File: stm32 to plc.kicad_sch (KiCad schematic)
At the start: 76 parts, among them J1 Microsemi_FlashPro-JTAG-10, J13 USB_C_Receptacle_USB2.0_14P, J14 Conn_01x08_Socket, J15 Conn_01x08_Socket, J16 Conn_2Rows-09Pins, J2 Conn_01x25, Q3 DMP3013SFV, Q4 BC107, Q5 BC107, SW1 SW_Push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

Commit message: :Zap:making chngs to powerinput, and relay output
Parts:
- removed BT1: Battery_Cell, symbol Device:Battery_Cell
- removed C12: 100nF, Capacitor_Tantalum_SMD:CP_EIA-3216-18_Kemet-A, symbol Device:C
- removed C13: 2.2uF, Capacitor_Tantalum_SMD:CP_EIA-3216-18_Kemet-A, symbol Device:C
- removed D6: PMEG3010EJ, Diode_SMD:D_SOD-323F, symbol Diode:PMEG3010EJ
- removed F1: Fuse, symbol Device:Fuse
- removed Q3: DMP3013SFV, Package_SON:Diodes_PowerDI3333-8, symbol Transistor_FET:DMP3013SFV
- removed R68: 10K, Resistor_SMD:R_0201_0603Metric, symbol Device:R
- added PS1: HLK-20M24, Converter_ACDC:Converter_ACDC_Hi-Link_HLK-20Mxx, symbol Converter_ACDC:HLK-20M24
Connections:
- net OUT 5V: no longer U2.2 (OUT)
- new net OUT 3.3V: U2.2 (OUT)

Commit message: :rocket:Have added Ethernet and removed USB
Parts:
- removed FB1: FerriteBead_Small, symbol Device:FerriteBead_Small
- removed J13: USB_C_Receptacle_USB2.0_14P, Connector_USB:USB_C_Receptacle_GCT_USB4105-xx-A_16P_TopMnt_Horizontal, symbol Connector:USB_C_Receptacle_USB2.0_14P
- removed R36, R37: 10k, Resistor_SMD:R_0805_2012Metric, symbol Device:R
- removed U8: CH340C, Package_SO:SOIC-16_3.9x9.9mm_P1.27mm, symbol Interface_USB:CH340C
- added C12, C13, C19: 100nF, Capacitor_SMD:C_0805_2012Metric, symbol Device:C
- added C17, C20: 10uF/10V, Capacitor_SMD:C_0805_2012Metric, symbol Device:C
- added L2: 22R /500MA, symbol Device:L
- added R13, R14: 10K, symbol Device:R
- added U8: LAN8720A, Package_DFN_QFN:VQFN-24-1EP_4x4mm_P0.5mm_EP2.5x2.5mm_ThermalVias, symbol Interface_Ethernet:LAN8720A
- C18: footprint Capacitor_Tantalum_SMD:CP_EIA-3216-18_Kemet-A -> Capacitor_SMD:C_0805_2012Metric
- R5: value 100K -> 12.1K/1%; footprint Resistor_SMD:R_0402_1005Metric -> (none)
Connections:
- net VCC_USB is gone; now on net GND: R5.2
- net +3.3V: no longer C18.1
- net -24V: now also PS1.3 (-Vout)
- net GND: now also C18.1, C5.2, C12.2, C13.1, C17.1, C19.1, C20.1, R14.2; no longer C18.2
- net GNDREF: no longer C5.2
- net RST: now also C18.2, R13.2, U8.15 (~{RST})
- net USB-CET: no longer R5.1
- net +3V3: now reaches C5.1
- net +3V3: now also C12.1, C13.2, C17.2, L2.2, R13.1
- net +24V: now reaches PS1.4 (+Vout)
- new net: C19.2, C20.2, U8.6 (VDDCR)
- new net: R5.1, U8.24 (RBIAS)
- new net +3V0: L2.1
- new net 3V3: U8.1 (VDD2A), U8.19 (VDD1A), U8.9 (VDDIO)
- new net CLK: U8.5 (XTAL1/CLKIN)
- new net LED SPD: U8.2 (LED2/~{INTSEL})
- new net LEDLINK: R14.1, U8.3 (LED1/REGOFF)
- new net MDC: U8.13 (MDC)
- new net MDIO: U8.12 (MDIO)
- new net PHYAD0: U8.10 (RXER/PHYAD0)
- new net RXD0: U8.8 (RXD0/MODE0)
- new net RXD1: U8.7 (RXD1/MODE1)
- new net RX_DV: U8.11 (CRS_DV/MODE2)
- new net RX_N: U8.22 (RXN)
- new net RX_P: U8.23 (RXP)
- new net TXD0: U8.17 (TXD0)
- new net TXD1: U8.18 (TXD1)
- new net TXEN: U8.16 (TXEN)
- new net TX_N: U8.20 (TXN)
- new net TX_P: U8.21 (TXP)
- new net XI: U8.4 (XTAL2)
- no-connect marks 14 -> 8
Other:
- note added: "ETHERNET"
- note removed: "USBC"
- moved on the sheet: J14, J15, J16, PS1, R66, R67

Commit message: :rocket:Have added Ethernet BUFFER and CONNECTED TO STM
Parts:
- removed J14, J15: Conn_01x08_Socket, Module:Flipper_Zero_Angled, symbol Connector:Conn_01x08_Socket
- removed J16: Conn_2Rows-09Pins, Module:Flipper_Zero_Straight, symbol Connector_Generic:Conn_2Rows-09Pins
- removed R66, R67: 10K, Resistor_SMD:R_0201_0603Metric, symbol Device:R
- added J3: RJ45_Hanrun_HR911105A_Horizontal, Connector_RJ:RJ45_Hanrun_HR911105A_Horizontal, symbol Connector:RJ45_Hanrun_HR911105A_Horizontal
- added R15, R16: 510R, Resistor_THT:R_Axial_DIN0309_L9.0mm_D3.2mm_P15.24mm_Horizontal, symbol Device:R
- added R17, R18, R19, R20: 49R9, symbol Device:R
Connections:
- net RX_DV is gone; now on net CRS_DV: U8.11 (CRS_DV/MODE2)
- net USBC_N is gone; now on net TXD0: U1.70 (PA11)
- net USBC_P is gone; now on net TXD1: U1.71 (PA12)
- net +3V3: now also J3.12, J3.4 (TCT), J3.5 (RCT), R17.2, R18.2, R19.1, R20.1
- net GND: now also J3.10
- net LED SPD: now also R16.2
- net LEDLINK: now also R15.2
- net MDC: now also U1.16 (PC1)
- net MDIO: now also U1.25 (PA2)
- net RXD0: now also U1.33 (PC4)
- net RXD1: now also U1.34 (PC5)
- net RX_N: now also J3.6 (RD-), R20.2
- net RX_P: now also J3.3 (RD+), R19.2
- net TXEN: now also U1.48 (PB11)
- net TX_N: now also J3.2 (TD-), R18.1
- net TX_P: now also J3.1 (TD+), R17.1
- net E_REF: now reaches U1.24 (PA1)
- net E_REF: now also U8.14 (~{INT}/REFCLKO)
- net CRS_DV: now reaches U1.32 (PA7)
- net USB-CET: no longer names the net of U1.68 (PA9)
- new net: J3.11, R16.1
- new net: J3.9, R15.1
- no-connect marks 8 -> 0
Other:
- note removed: "SPI"
- moved on the sheet: C10, C11, C12, C13, C14, C15, C16, C17, C18, C19, C20, C24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

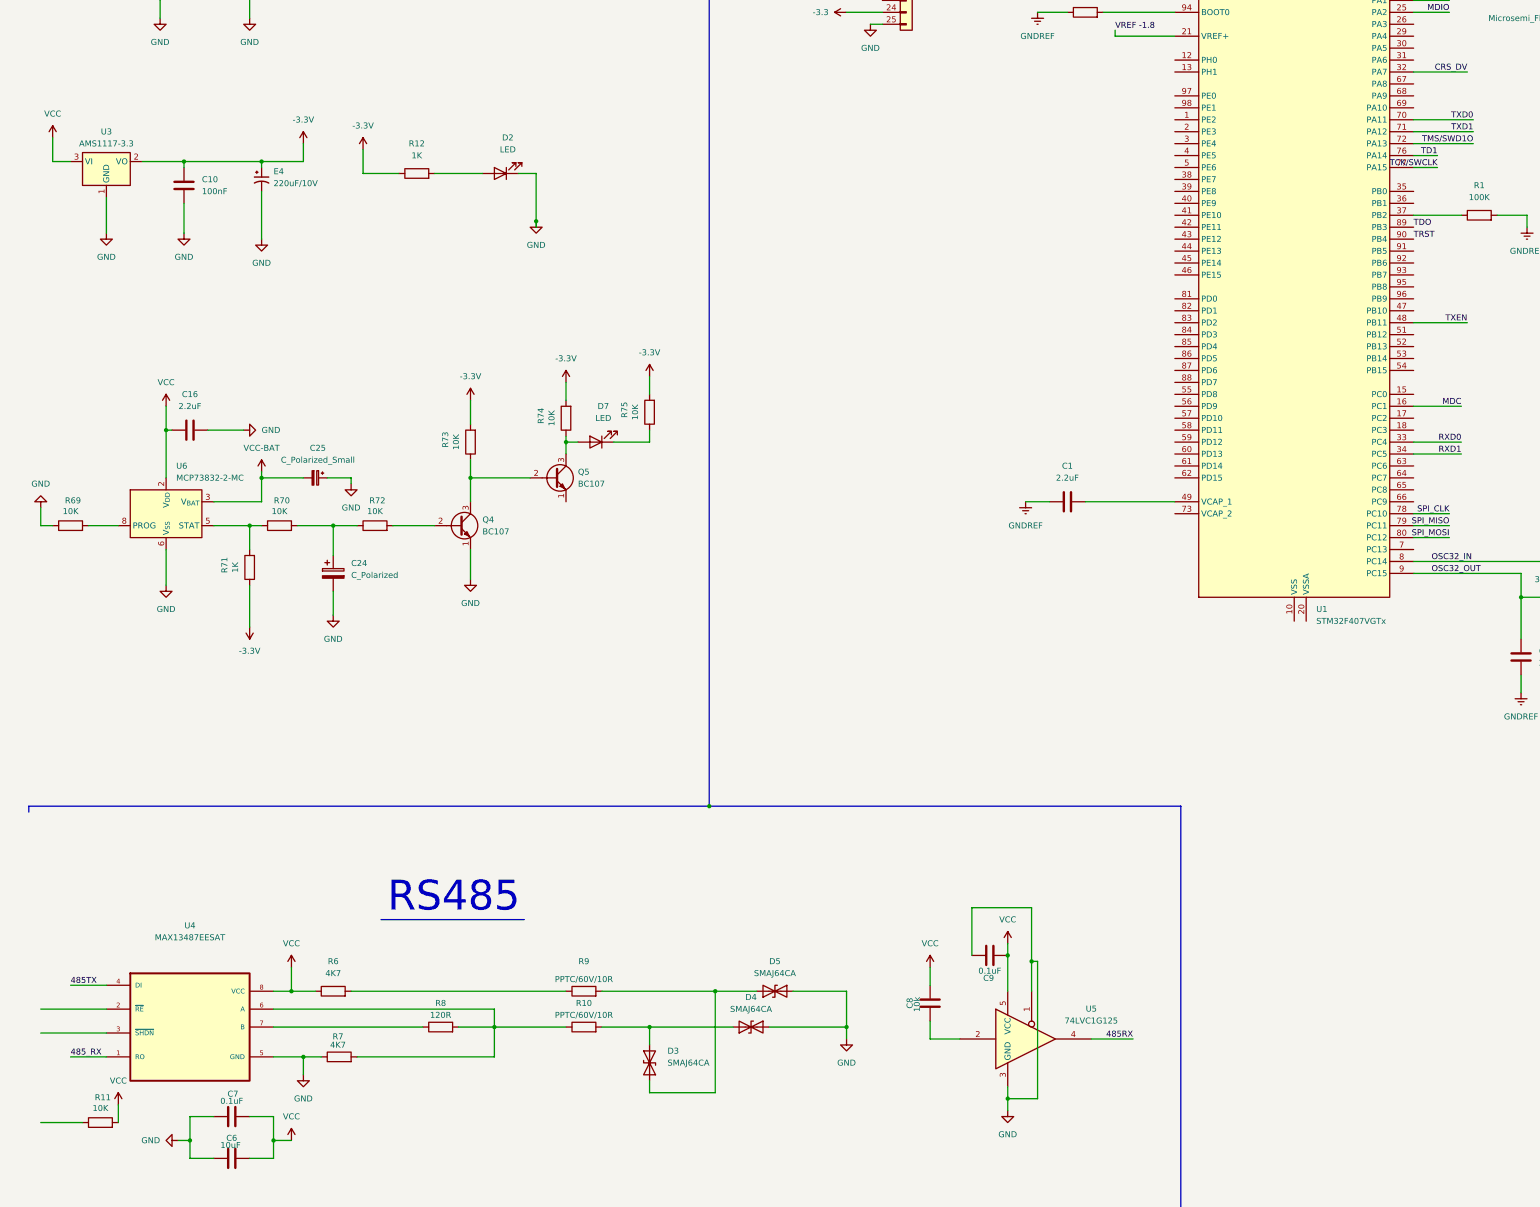
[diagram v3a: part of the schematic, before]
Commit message: :wrench: Connecting opto to the relay
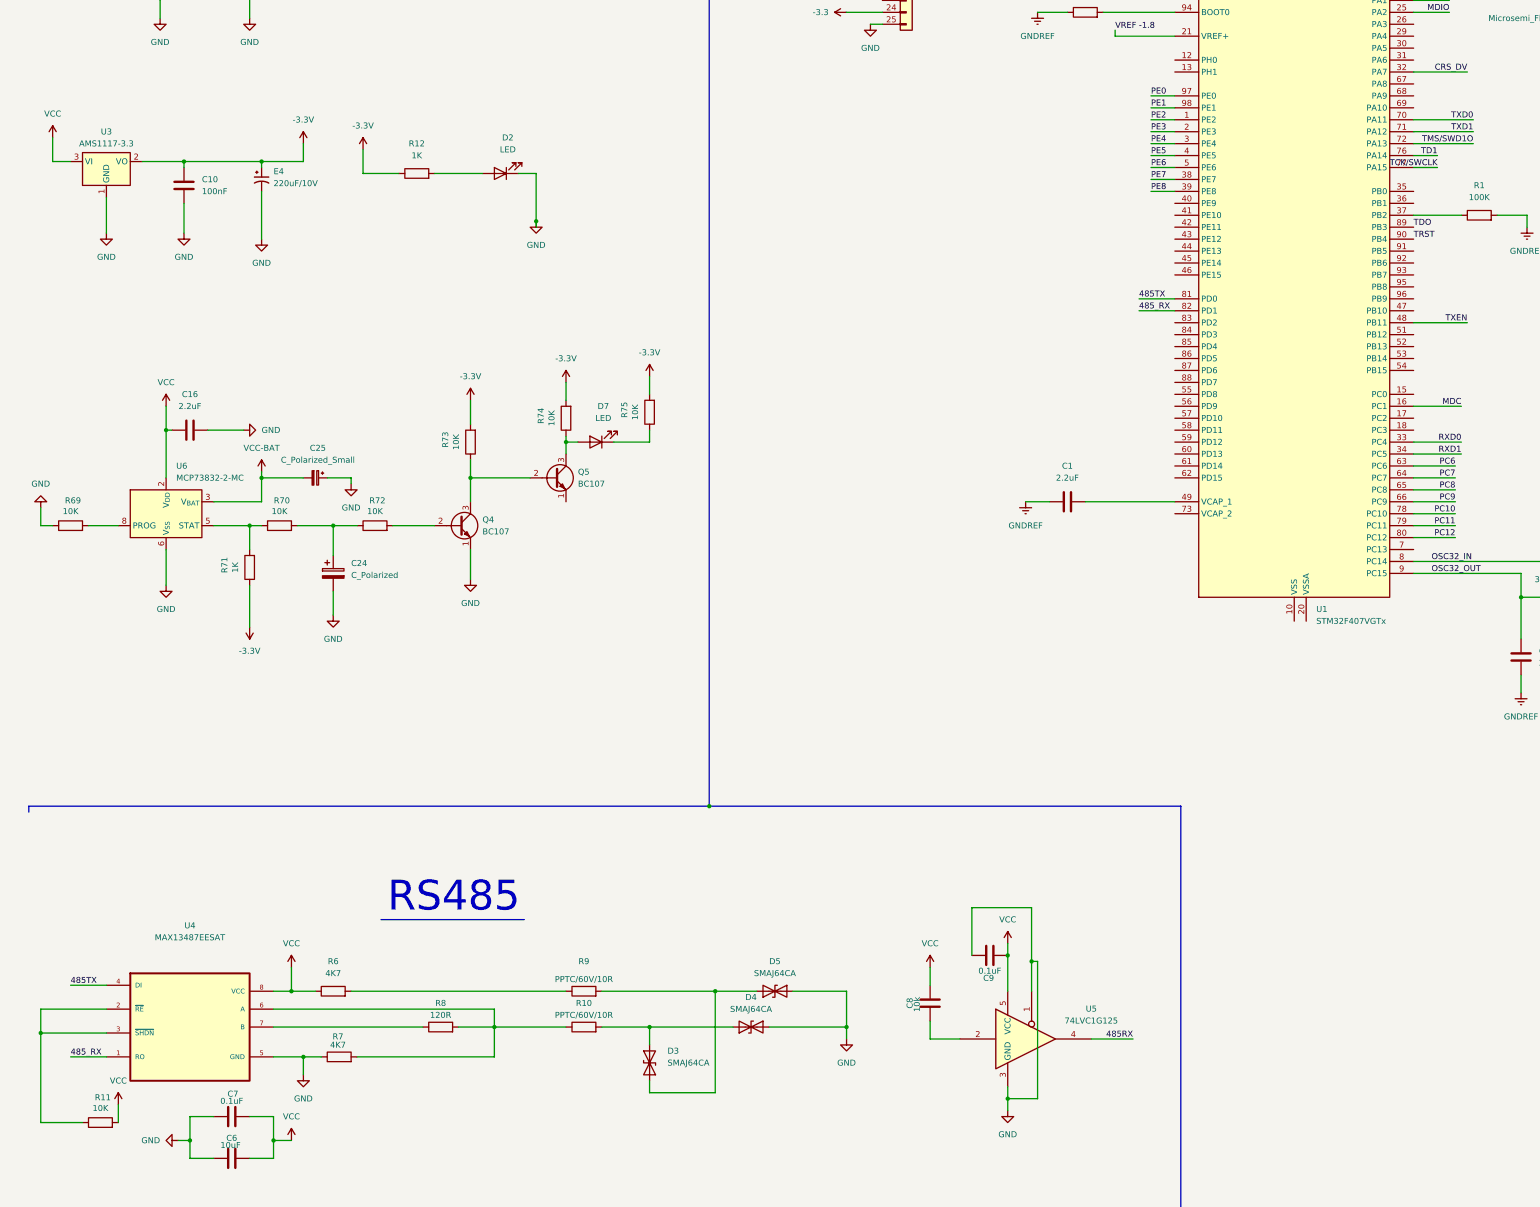
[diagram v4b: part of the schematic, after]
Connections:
- net 485TX: now also U1.81 (PD0)
- net 485_RX: now also U1.82 (PD1)
- net SPI_CLK: no longer U1.78 (PC10)
- net SPI_MISO: no longer U1.79 (PC11)
- net SPI_MOSI: no longer U1.80 (PC12)
- net PE2: now reaches U1.1 (PE2)
- net PE3: now reaches U1.2 (PE3)
- net PE4: now reaches U1.3 (PE4)
- net PE7: now reaches U1.38 (PE7)
- net PE8: now reaches U1.39 (PE8)
- net PE5: now reaches U1.4 (PE5)
- net PE6: now reaches U1.5 (PE6)
- net PC6: now reaches U1.63 (PC6)
- net PC7: now reaches U1.64 (PC7)
- net PC8: now reaches U1.65 (PC8)
- net PC9: now reaches U1.66 (PC9)
- net PE0: now reaches U1.97 (PE0)
- net PE1: now reaches U1.98 (PE1)
- net at U4.2 (~{RE}): now also R11.1, U4.3 (~{SHDN})
- new net PC10: U1.78 (PC10)
- new net PC11: U1.79 (PC11)
- new net PC12: U1.80 (PC12)

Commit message: :tada: Completing minor touches
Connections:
- net IN_D5: now reaches U1.55 (PD8)
- net IN_D6: now reaches U1.56 (PD9)
- net IN_D1: now reaches U1.85 (PD4)
- net IN_D2: now reaches U1.86 (PD5)
- net IN_D3: now reaches U1.87 (PD6)
- net IN_D4: now reaches U1.88 (PD7)
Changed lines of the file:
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@@
+	(wire
+		(pts
+			(xy 248.92 205.74) (xy 257.81 205.74)
+		)
+		(stroke
+			(width 0)
+			(type default)
+		)
+	)
 	(wire
 		(pts
@@
 	(wire
 		(pts
+			(xy 248.92 218.44) (xy 257.81 218.44)
+		)
+		(stroke
+			(width 0)
+			(type default)
+		)
+	)
+	(wire
+		(pts
 			(xy 66.04 346.71) (xy 113.03 346.71)
 		)
@@
 	(wire
 		(pts
+			(xy 248.92 210.82) (xy 257.81 210.82)
+		)
+		(stroke
+			(width 0)
+			(type default)
+		)
+	)
+	(wire
+		(pts
 			(xy 245.11 129.54) (xy 245.11 128.27)
 		)
@@
 	(wire
 		(pts
+			(xy 248.92 213.36) (xy 257.81 213.36)
+		)
+		(stroke
+			(width 0)
+			(type default)
+		)
+	)
+	(wire
+		(pts
 			(xy 53.34 378.46) (xy 48.26 378.46)
 		)
@@
 	(wire
 		(pts
+			(xy 248.92 208.28) (xy 257.81 208.28)
+		)
+		(stroke
+			(width 0)
+			(type default)
+		)
+	)
+	(wire
+		(pts
 			(xy 246.38 62.23) (xy 246.38 69.85)
 		)
@@
 		(pts
 			(xy 308.61 160.02) (xy 321.31 160.02)
+		)
+		(stroke
+			(width 0)
+			(type default)
+		)
+	)
+	(wire
+		(pts
+			(xy 248.92 215.9) (xy 257.81 215.9)
 		)
 		(stroke
@@
 		)
 	)
+	(label "IN_D6"
+		(at 248.92 218.44 0)
+		(effects
+			(font
+				(size 1.27 1.27)
+			)
+			(justify left bottom)
+		)
+	)
 	(label "TXEN"
 		(at 469.9 93.98 0)
@@
 		)
 	)
+	(label "IN_D1"
+		(at 248.92 205.74 0)
+		(effects
+			(font
+				(size 1.27 1.27)
+			)
+			(justify left bottom)
+		)
+	)
 	(label "PC10"
 		(at 317.5 241.3 180)
@@
 		)
 	)
+	(label "IN_D5"
+		(at 248.92 215.9 0)
+		(effects
+			(font
+				(size 1.27 1.27)
+			)
+			(justify left bottom)
+		)
+	)
 	(label "RX_P"
 		(at 431.8 232.41 0)
@@
 		)
 	)
+	(label "IN_D3"
+		(at 248.92 210.82 0)
+		(effects
+			(font
+				(size 1.27 1.27)
+			)
+			(justify left bottom)
+		)
+	)
 	(label "485TX"
 		(at 22.86 341.63 0)
@@
 		)
 	)
+	(label "IN_D4"
+		(at 248.92 213.36 0)
+		(effects
+			(font
+				(size 1.27 1.27)
+			)
+			(justify left bottom)
+		)
+	)
 	(label "RX_N"
 		(at 431.8 237.49 0)
@@
 		)
 	)
+	(label "IN_D2"
+		(at 248.92 208.28 0)
+		(effects
+			(font
+				(size 1.27 1.27)
+			)
+			(justify left bottom)
+		)
+	)
